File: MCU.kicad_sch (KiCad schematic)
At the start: 10 parts, among them SW1 SW_Omron_B3FS, SW3 SW_Omron_B3FS, U1 ESP32-WROOM-32E, X1 SG-3030CM

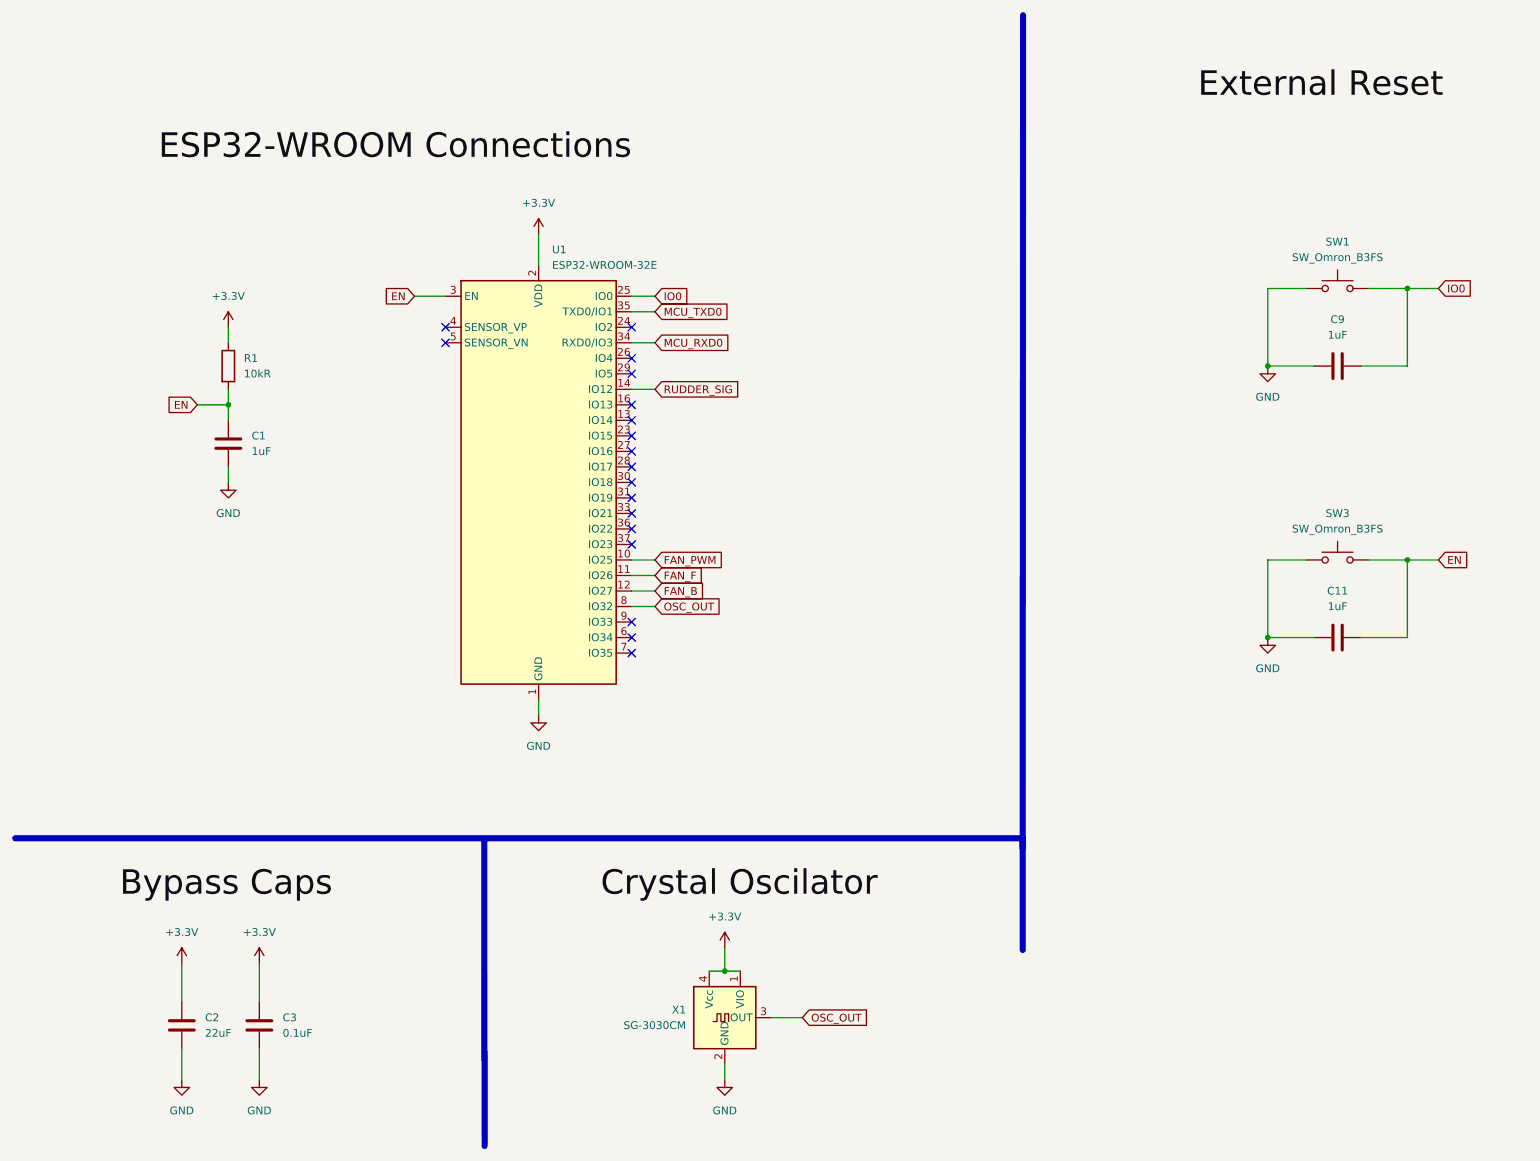
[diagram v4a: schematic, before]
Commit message: Updated to use boost converters
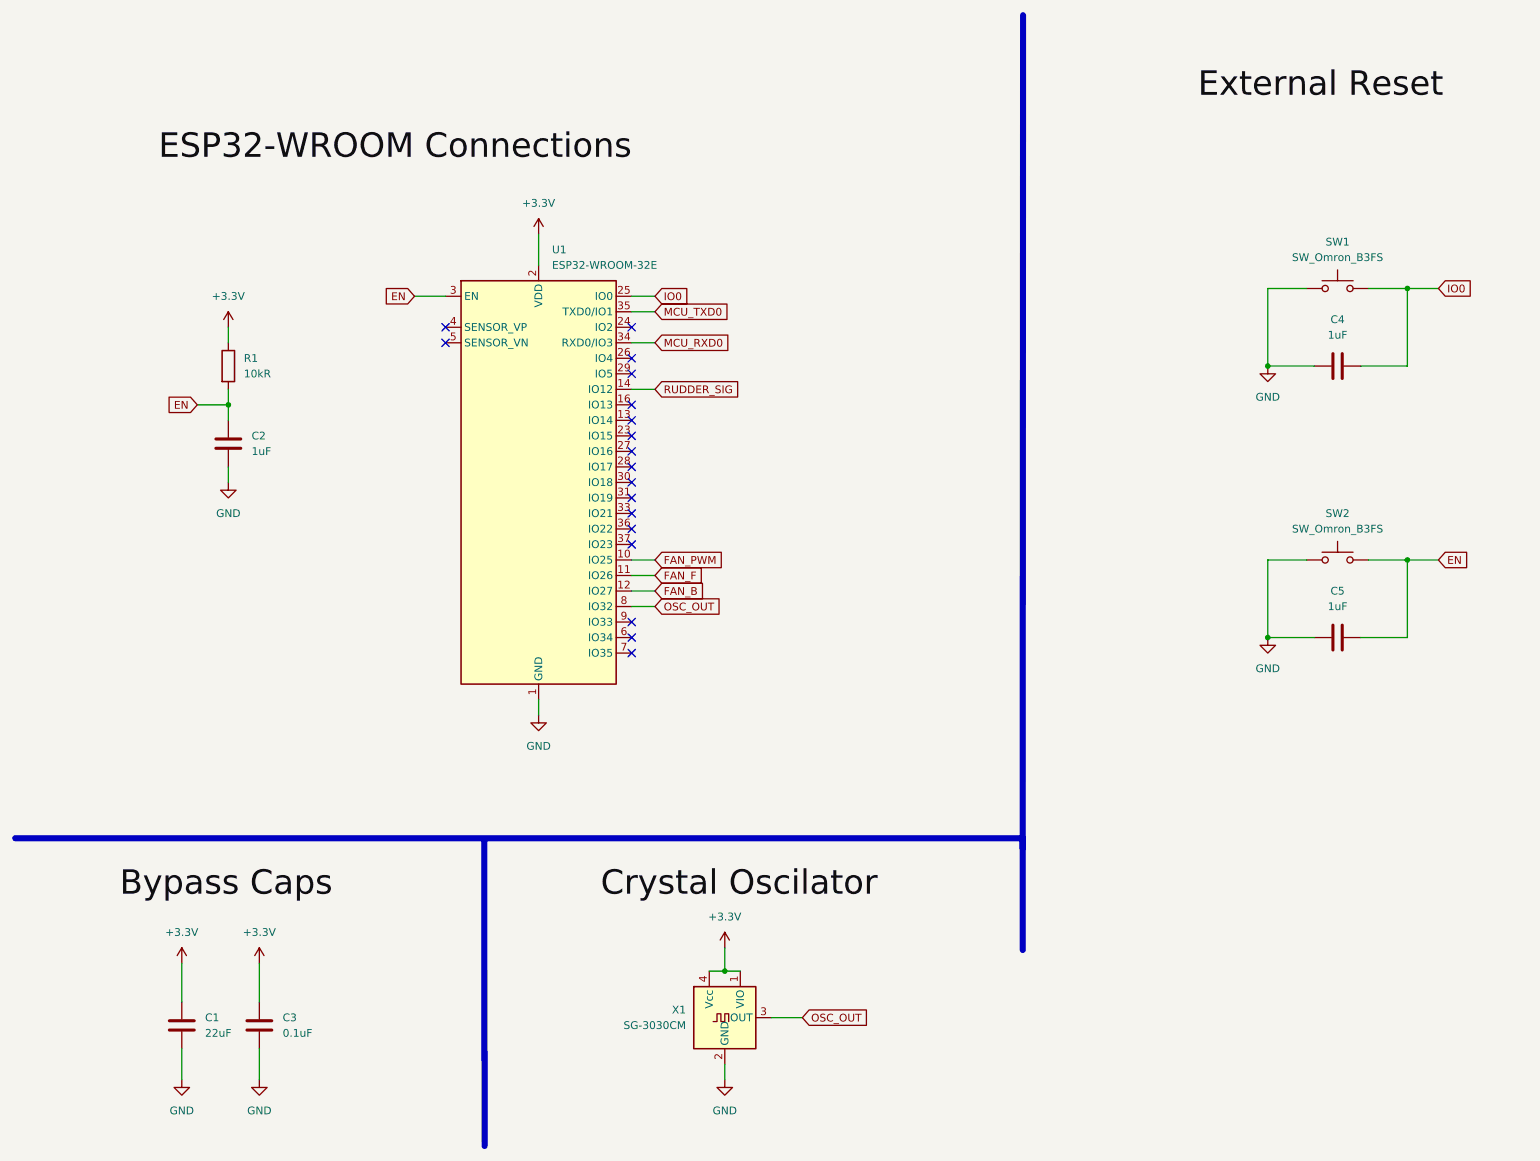
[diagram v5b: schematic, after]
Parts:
- renumbered C2 to C1, C1 to C2, C9 to C4, C11 to C5, SW3 to SW2
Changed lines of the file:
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@@
 		(dnp no)
 		(fields_autoplaced yes)
-		(property "Reference" "C1"
+		(property "Reference" "C2"
 			(at 50.8 81.2799 0)
 			(effects
@@
 			(project "Airboat"
 				(path "/32966cbd-337b-4fa7-b66f-bfe62b1c18c3/02e382f4-e1e7-4e1b-a73d-e36f8e3f186b"
-					(reference "C1")
+					(reference "C2")
 					(unit 1)
 				)
@@
 			(project ""
 				(path "/a772d62b-9e8d-42e3-92d7-059cff83940a"
-					(reference "C1")
+					(reference "C?")
 					(unit 1)
 				)
@@
 		(dnp no)
 		(fields_autoplaced yes)
-		(property "Reference" "#PWR06"
+		(property "Reference" "#PWR09"
 			(at 128.27 168.91 0)
 			(effects
@@
 			(project "Airboat"
 				(path "/32966cbd-337b-4fa7-b66f-bfe62b1c18c3/02e382f4-e1e7-4e1b-a73d-e36f8e3f186b"
-					(reference "#PWR06")
+					(reference "#PWR09")
 					(unit 1)
 				)
@@
 		(dnp no)
 		(fields_autoplaced yes)
-		(property "Reference" "#PWR05"
+		(property "Reference" "#PWR010"
 			(at 128.27 193.04 0)
 			(effects
@@
 			(project "Airboat"
 				(path "/32966cbd-337b-4fa7-b66f-bfe62b1c18c3/02e382f4-e1e7-4e1b-a73d-e36f8e3f186b"
-					(reference "#PWR05")
+					(reference "#PWR010")
 					(unit 1)
 				)
@@
 		(dnp no)
 		(fields_autoplaced yes)
-		(property "Reference" "#PWR07"
+		(property "Reference" "#PWR01"
 			(at 39.37 171.45 0)
 			(effects
@@
 			(project "Airboat"
 				(path "/32966cbd-337b-4fa7-b66f-bfe62b1c18c3/02e382f4-e1e7-4e1b-a73d-e36f8e3f186b"
-					(reference "#PWR07")
+					(reference "#PWR01")
 					(unit 1)
 				)
@@
 		(dnp no)
 		(fields_autoplaced yes)
-		(property "Reference" "#PWR09"
+		(property "Reference" "#PWR06"
 			(at 52.07 193.04 0)
 			(effects
@@
 			(project "Airboat"
 				(path "/32966cbd-337b-4fa7-b66f-bfe62b1c18c3/02e382f4-e1e7-4e1b-a73d-e36f8e3f186b"
-					(reference "#PWR09")
+					(reference "#PWR06")
 					(unit 1)
 				)
@@
 		(dnp no)
 		(fields_autoplaced yes)
-		(property "Reference" "#PWR042"
+		(property "Reference" "#PWR012"
 			(at 217.17 120.65 0)
 			(effects
@@
 			(project "Airboat"
 				(path "/32966cbd-337b-4fa7-b66f-bfe62b1c18c3/02e382f4-e1e7-4e1b-a73d-e36f8e3f186b"
-					(reference "#PWR042")
+					(reference "#PWR012")
 					(unit 1)
 				)
@@
 		(dnp no)
 		(fields_autoplaced yes)
-		(property "Reference" "#PWR043"
+		(property "Reference" "#PWR011"
 			(at 217.17 76.2 0)
 			(effects
@@
 			(project "Airboat"
 				(path "/32966cbd-337b-4fa7-b66f-bfe62b1c18c3/02e382f4-e1e7-4e1b-a73d-e36f8e3f186b"
-					(reference "#PWR043")
+					(reference "#PWR011")
 					(unit 1)
 				)
@@
 		(dnp no)
 		(fields_autoplaced yes)
-		(property "Reference" "#PWR02"
+		(property "Reference" "#PWR08"
 			(at 97.79 133.35 0)
 			(effects
@@
 			(project "Airboat"
 				(path "/32966cbd-337b-4fa7-b66f-bfe62b1c18c3/02e382f4-e1e7-4e1b-a73d-e36f8e3f186b"
-					(reference "#PWR02")
+					(reference "#PWR08")
 					(unit 1)
 				)
@@
 			(project ""
 				(path "/a772d62b-9e8d-42e3-92d7-059cff83940a"
-					(reference "#PWR02")
+					(reference "#PWR?")
 					(unit 1)
 				)
@@
 		(dnp no)
 		(fields_autoplaced yes)
-		(property "Reference" "C11"
+		(property "Reference" "C5"
 			(at 228.6 106.68 90)
 			(effects
@@
 			(project "Airboat"
 				(path "/32966cbd-337b-4fa7-b66f-bfe62b1c18c3/02e382f4-e1e7-4e1b-a73d-e36f8e3f186b"
-					(reference "C11")
+					(reference "C5")
 					(unit 1)
 				)
@@
 		(dnp no)
 		(fields_autoplaced yes)
-		(property "Reference" "#PWR08"
+		(property "Reference" "#PWR05"
 			(at 52.07 171.45 0)
 			(effects
@@
 			(project "Airboat"
 				(path "/32966cbd-337b-4fa7-b66f-bfe62b1c18c3/02e382f4-e1e7-4e1b-a73d-e36f8e3f186b"
-					(reference "#PWR08")
+					(reference "#PWR05")
 					(unit 1)
 				)
@@
 		(on_board yes)
 		(dnp no)
-		(property "Reference" "#PWR01"
+		(property "Reference" "#PWR07"
 			(at 97.79 52.07 0)
 			(effects
@@
 			(project "Airboat"
 				(path "/32966cbd-337b-4fa7-b66f-bfe62b1c18c3/02e382f4-e1e7-4e1b-a73d-e36f8e3f186b"
-					(reference "#PWR01")
+					(reference "#PWR07")
 					(unit 1)
 				)
@@
 		(dnp no)
 		(fields_autoplaced yes)
-		(property "Reference" "#PWR010"
+		(property "Reference" "#PWR02"
 			(at 39.37 193.04 0)
 			(effects
@@
 			(project "Airboat"
 				(path "/32966cbd-337b-4fa7-b66f-bfe62b1c18c3/02e382f4-e1e7-4e1b-a73d-e36f8e3f186b"
-					(reference "#PWR010")
+					(reference "#PWR02")
 					(unit 1)
 				)
@@
 		(dnp no)
 		(fields_autoplaced yes)
-		(property "Reference" "C2"
+		(property "Reference" "C1"
 			(at 43.18 176.5299 0)
 			(effects
@@
 			(project "Airboat"
 				(path "/32966cbd-337b-4fa7-b66f-bfe62b1c18c3/02e382f4-e1e7-4e1b-a73d-e36f8e3f186b"
-					(reference "C2")
+					(reference "C1")
 					(unit 1)
 				)
@@
 		(dnp no)
 		(fields_autoplaced yes)
-		(property "Reference" "C9"
+		(property "Reference" "C4"
 			(at 228.6 62.23 90)
 			(effects
@@
 			(project "Airboat"
 				(path "/32966cbd-337b-4fa7-b66f-bfe62b1c18c3/02e382f4-e1e7-4e1b-a73d-e36f8e3f186b"
-					(reference "C9")
+					(reference "C4")
 					(unit 1)
 				)
@@
 			(project ""
 				(path "/a772d62b-9e8d-42e3-92d7-059cff83940a"
-					(reference "X1")
+					(reference "X?")
 					(unit 1)
 				)
@@
 		(dnp no)
 		(fields_autoplaced yes)
-		(property "Reference" "SW3"
+		(property "Reference" "SW2"
 			(at 228.6 93.98 0)
 			(effects
@@
 			(project "Airboat"
 				(path "/32966cbd-337b-4fa7-b66f-bfe62b1c18c3/02e382f4-e1e7-4e1b-a73d-e36f8e3f186b"
-					(reference "SW3")
+					(reference "SW2")
 					(unit 1)
 				)
@@
 			(project ""
 				(path "/a772d62b-9e8d-42e3-92d7-059cff83940a"
-					(reference "R1")
-					(unit 1)
-				)
+					(reference "R?")
+					(unit 1)
+				)
